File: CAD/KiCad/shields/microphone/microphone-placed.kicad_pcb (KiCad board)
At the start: 2 copper layers, 20 x 62 mm, 23 parts, among them J1 GND / +5V / OUT, U1 MAX9814ETD+

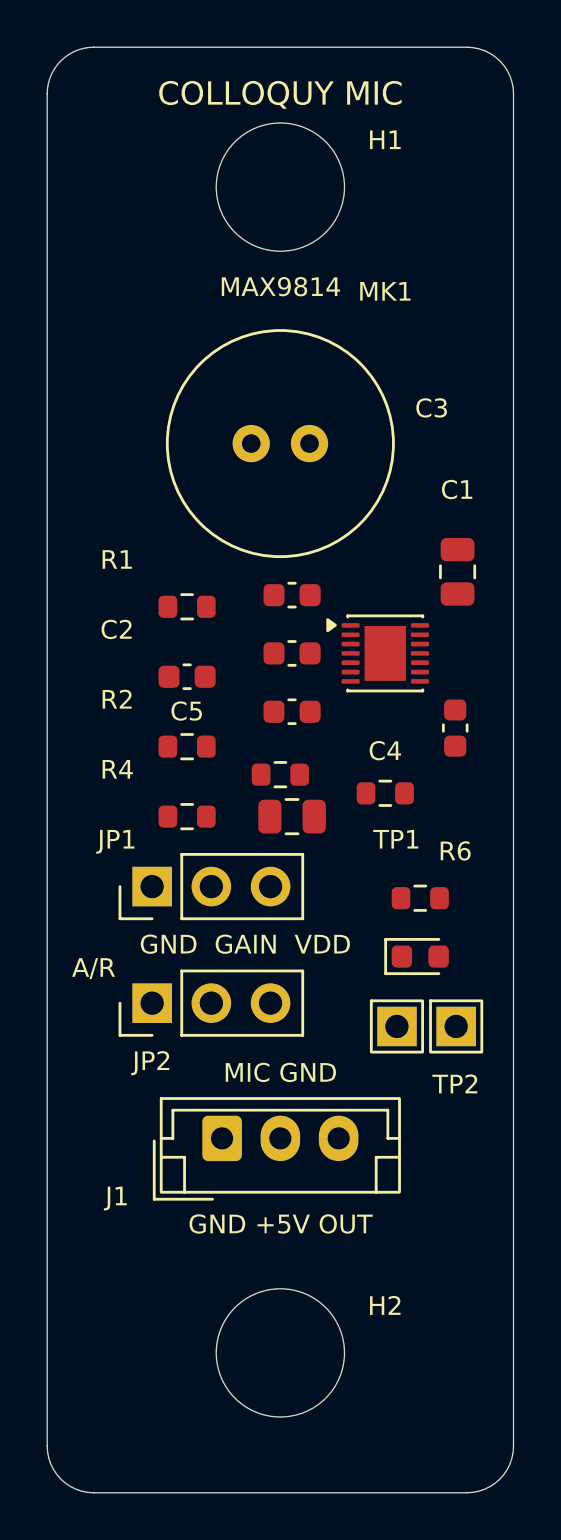
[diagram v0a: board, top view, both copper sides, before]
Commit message: Mount the MAX9814 module on a socketed artwork holder
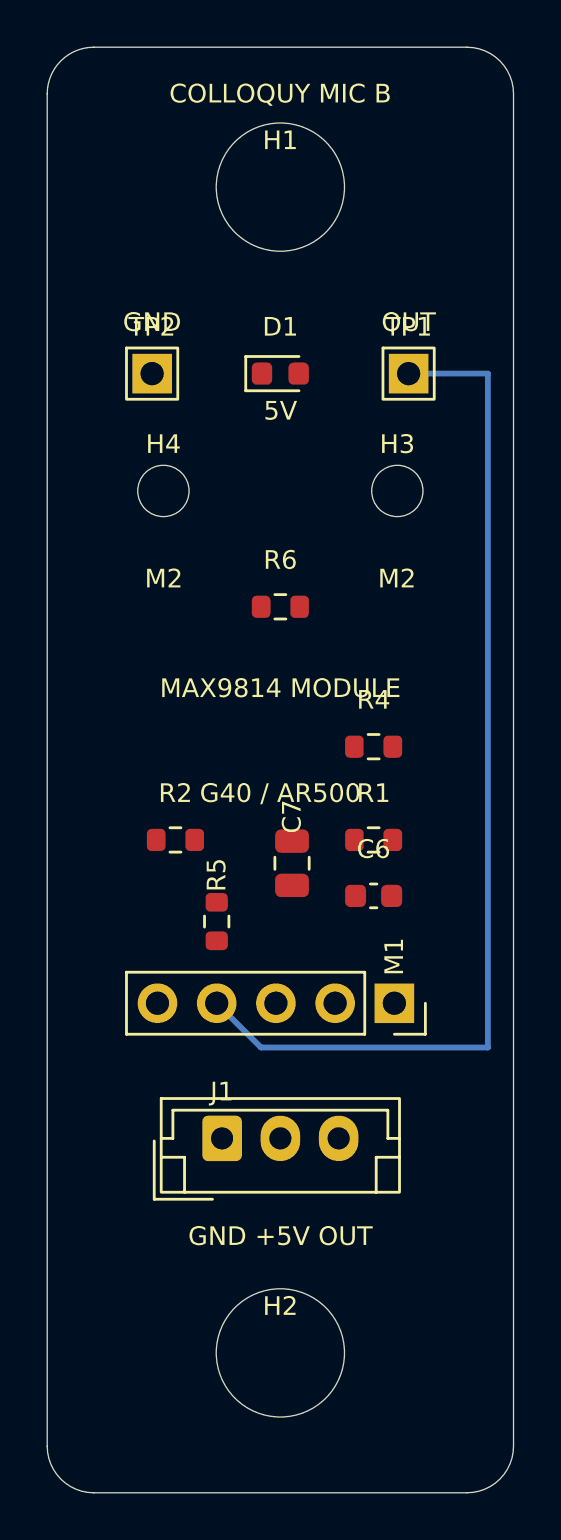
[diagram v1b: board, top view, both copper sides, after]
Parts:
- removed C1: 100nF C0G, Shields:C_0805_2012Metric
- removed C2, C4: 470nF X7R, Shields:C_0603_1608Metric
- removed C3: 2.2uF X5R, Shields:C_0603_1608Metric
- removed C5: 1uF, Shields:C_0603_1608Metric
- removed JP1: FIT 2-3: 40dB, Shields:PinHeader_1x03_P2.54mm_Vertical
- removed JP2: FIT 1-2: 1:500, Shields:PinHeader_1x03_P2.54mm_Vertical
- removed MK1: 9.7mm electret -44dB, Shields:Electret_9.7mm_P2.5mm
- removed R3: 100K, Shields:R_0603_1608Metric
- removed U1: MAX9814ETD+, Shields:TDFN-14-1EP_3x3mm_P0.4mm_EP1.78x2.35mm
- added H3: M2 MODULE / INSULATING SPACER, Shields:MountingHole_2.2mm_M2_Keepout6, F.Cu at (65.0, 69.0)
- added H4: M2 MODULE / INSULATING SPACER, Shields:MountingHole_2.2mm_M2_Keepout6, F.Cu at (55.0, 69.0)
- added M1: MAX9814 MODULE / 1x05 SOCKET, Shields:MAX9814_Module_Socket_1x05, F.Cu at (64.9, 91.0)
- R1: value 2K21 -> 0R / GAIN VDD 40dB
- R2: value 150K -> 0R / AR GND 1:500
- moved TP2 30.9 mm to (54.5, 64.0)
- moved TP1 28.0 mm to (65.5, 64.0)
- moved D1 25.7 mm to (60.0, 64.0)
- moved R6 13.9 mm to (60.0, 74.0)
- moved R1 12.8 mm to (64.0, 84.0)
- moved R5 9.08 mm to (57.3, 87.5), turned to 90 degrees
- moved C6 8.64 mm to (64.0, 86.4)
- moved R4 8.54 mm to (64.0, 80.0)
- moved R2 4.03 mm to (55.5, 84.0)
- moved C7 2.00 mm to (60.5, 85.0), turned to 90 degrees
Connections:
- net led/D1 renamed led/D1
- R1 pad 1: MICBIAS -> GAIN
- R1 pad 2: MIC_POS -> VDD
- R2 pad 1: MICBIAS -> AR
- R2 pad 2: TH -> GND
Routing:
- net MICOUT: track 0.00 -> 44.7 mm
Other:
- board text added: "5V"
- board text added: "COLLOQUY MIC B"
- board text added: "G40 / AR500"
- board text added: "GND"
- board text added: "GND VDD GAIN"
- board text added: "M2"
- board text added: "M2 NYLON POSTS"
- board text added: "M5 / INSULATE FRAME"
- board text added: "MATCH SOCKET HEIGHT"
- board text added: "MAX9814 MODULE"
- board text added: "MODULE ABOVE / FACE ROOM"
- board text added: "OUT"
- board text added: "OUT AR / 1x5"
- board text added: "VIOLET MODULE"
- board text removed: "40dB: GAIN-VDD 50dB: GAIN-GND 60dB: OPEN A/R: GND = 1:500 VDD = 1:2000 OPEN = 1:4000"
- board text removed: "A/R"
- board text removed: "COLLOQUY MIC"
- board text removed: "GND GAIN VDD"
- board text removed: "M5 / NYLON INSULATE FRAME"
- board text removed: "MAX9814"
- board text removed: "MIC GND"
